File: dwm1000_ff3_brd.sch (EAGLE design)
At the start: 19 parts, among them J3 AVR_SPI_PRG_6PTH

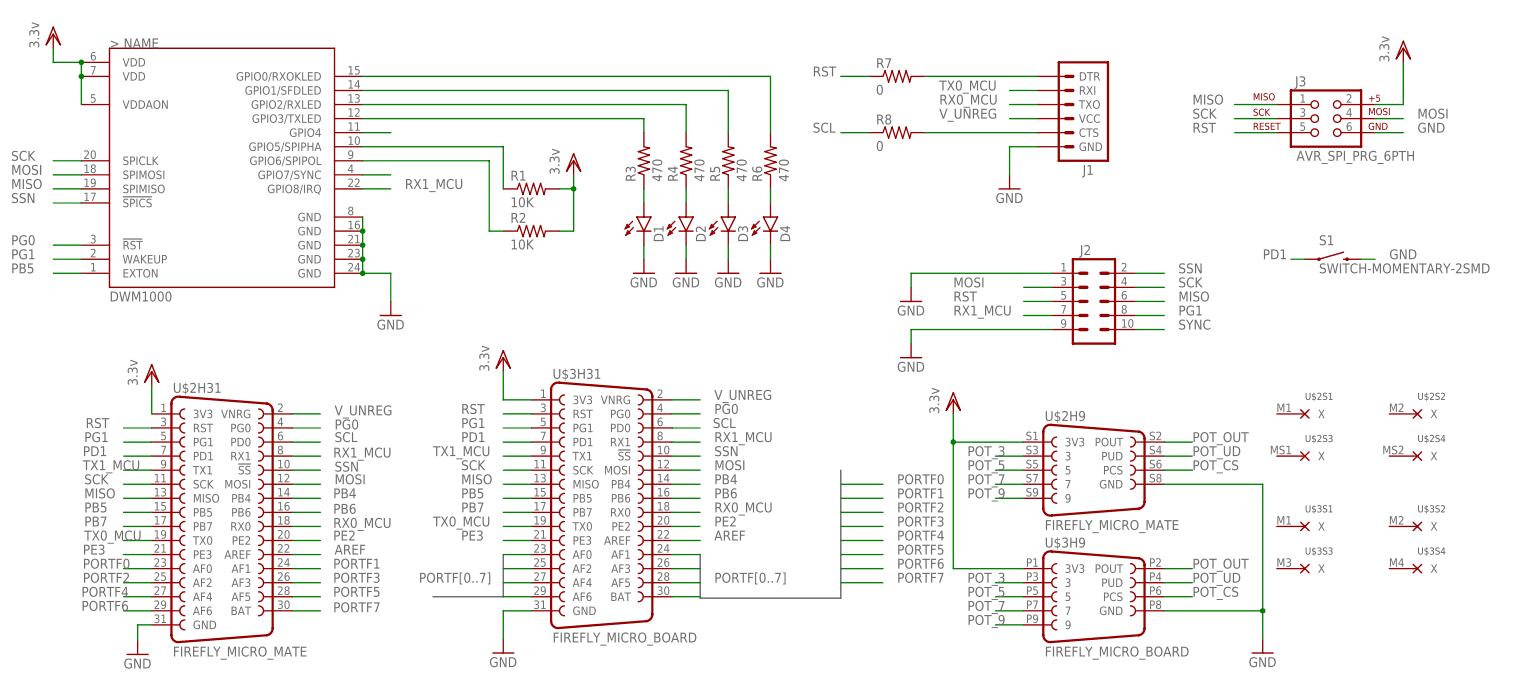
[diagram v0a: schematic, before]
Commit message: added firefly DWM1000 module
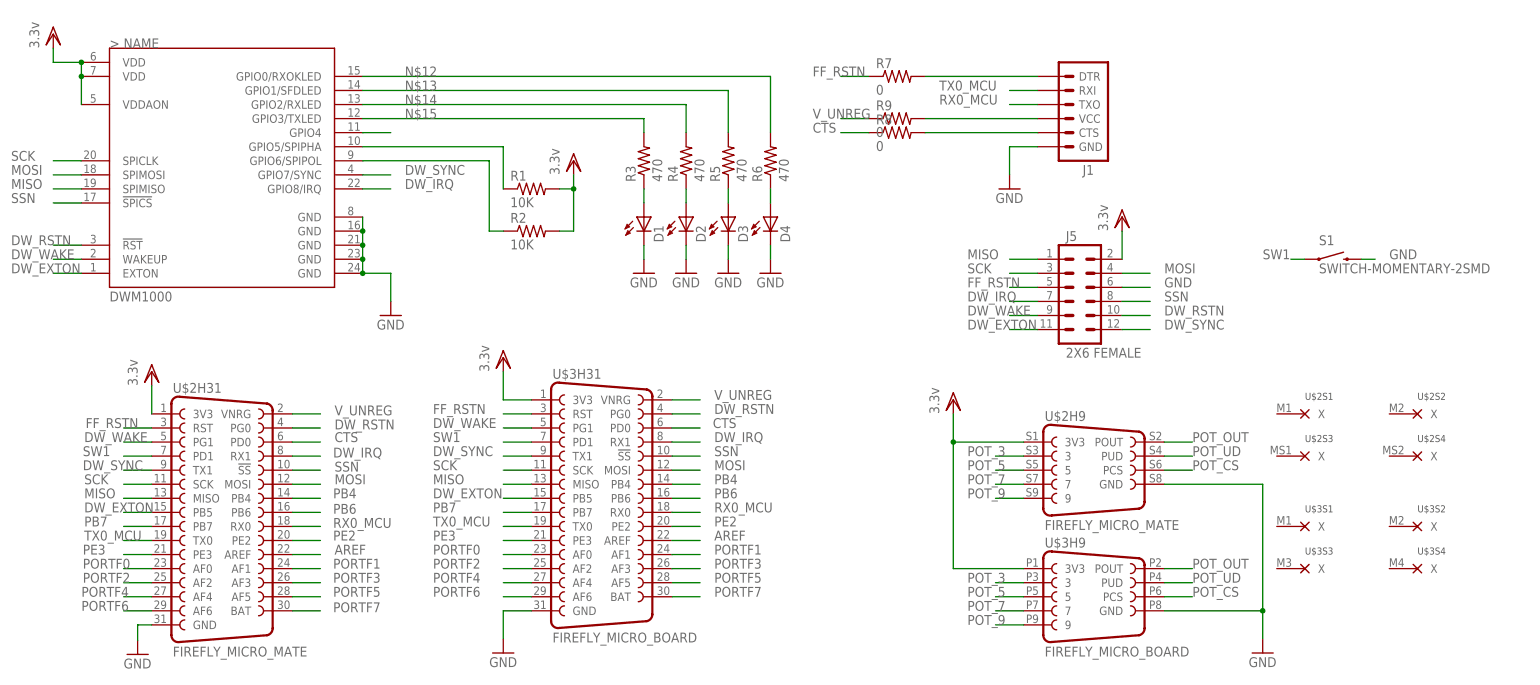
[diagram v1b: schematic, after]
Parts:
- removed J2: (no value), SparkFun-Connectors:M05X2SHD
- removed J3: AVR_SPI_PRG_6PTH, SparkFun-Connectors:AVR_SPI_PRG_6PTH
- added J5: 2X6 FEMALE, SparkFun-Connectors:M06X2PTH_FEMALE
- added R9: 0, rcl:R-US_R0603
- D1, D2, D3, D4: device SparkFun-LED:LED1206 -> led:LEDCHIP-LED0603
- R1, R2, R3, R4, R5, R6, R7, R8: device SparkFun-Passives:RESISTOR1206 -> rcl:R-US_R0603
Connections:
- net PD1 renamed SW1
- net SCL renamed CTS
- removed net N$11: U$1.GPIO7/SYNC
- removed net PB5: U$1.EXTON, U$2H31.PB5, U$3H31.PB5
- removed net PG0: U$1.!RST, U$2H31.PG0, U$3H31.PG0
- removed net PG1: J2.8, U$1.WAKEUP, U$2H31.PG1, U$3H31.PG1
- removed net RST: J2.5, J3.5, R7.1, U$2H31.RST, U$3H31.RST
- removed net RX1_MCU: J2.7, U$1.GPIO8/IRQ, U$2H31.RX1, U$3H31.RX1
- removed net SYNC: J2.10
- removed net TX1_MCU: U$2H31.TX1, U$3H31.TX1
- new net DW_EXTON: J5.11, U$1.EXTON, U$2H31.PB5, U$3H31.PB5
- new net DW_IRQ: J5.7, U$1.GPIO8/IRQ, U$2H31.RX1, U$3H31.RX1
- new net DW_RSTN: J5.10, U$1.!RST, U$2H31.PG0, U$3H31.PG0
- new net DW_SYNC: J5.12, U$1.GPIO7/SYNC, U$2H31.TX1, U$3H31.TX1
- new net DW_WAKE: J5.9, U$1.WAKEUP, U$2H31.PG1, U$3H31.PG1
- new net FF_RSTN: J5.5, R7.1, U$2H31.RST, U$3H31.RST
- new net N$6: J1.VCC, R9.2
- net GND: now also J5.6; no longer J2.1, J2.9, J3.6
- net MISO: now also J5.1; no longer J2.6, J3.1
- net MOSI: now also J5.4; no longer J2.3, J3.4
- net SCK: now also J5.3; no longer J2.4, J3.3
- net SSN: now also J5.8; no longer J2.2
- net VDD: now also J5.2; no longer J3.2
- net V_UNREG: now also R9.1; no longer J1.VCC
